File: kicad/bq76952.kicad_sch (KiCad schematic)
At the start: 88 parts, among them Q1 DMN10H220LE, U4 BQ76952

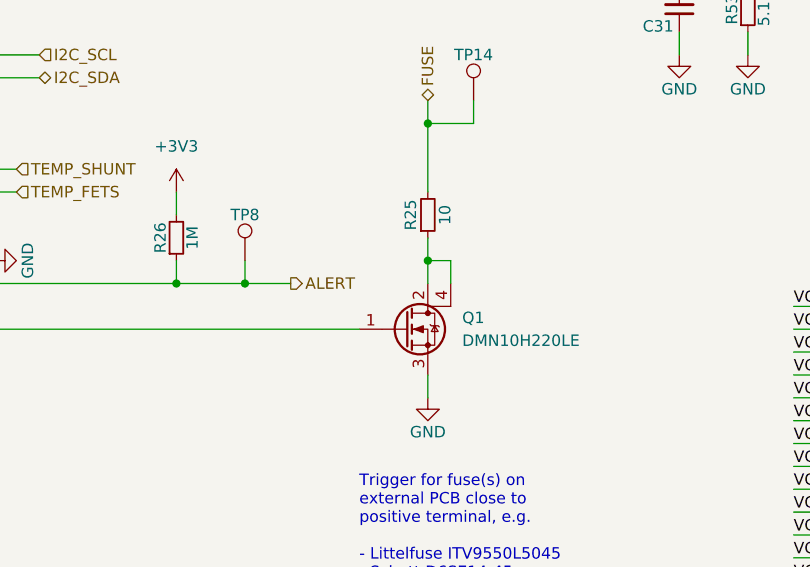
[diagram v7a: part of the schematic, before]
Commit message: Create cost-optimized Lite variant of the BMS C1 v0.4.1
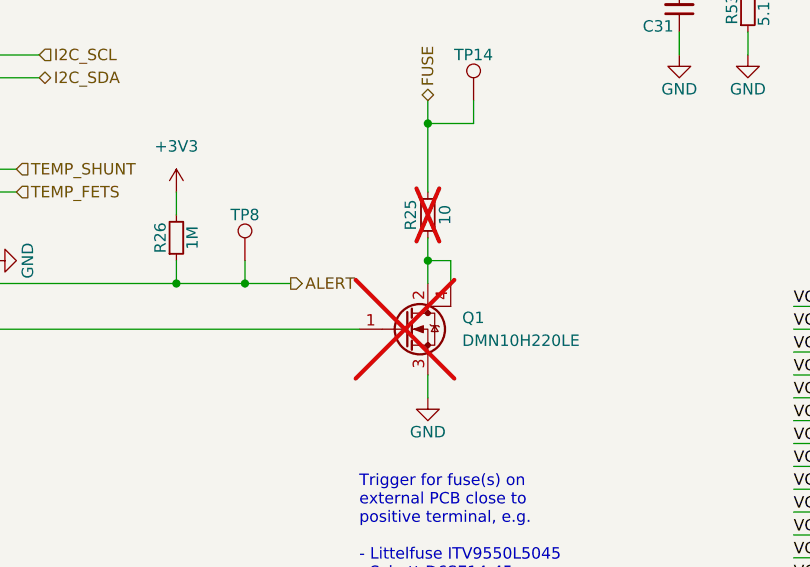
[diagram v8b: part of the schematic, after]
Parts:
- Q1, R25: now not fitted
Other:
- title: Libre Solar BMS C1 -> Libre Solar BMS C1 lite
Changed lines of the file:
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@@
 	(paper "A4")
 	(title_block
-		(title "Libre Solar BMS C1")
+		(title "Libre Solar BMS C1 lite")
 		(date "2024-03-17")
 		(rev "0.4.1")
@@
 		(exclude_from_sim no)
 		(in_bom yes)
-		(on_board yes)
-		(dnp no)
+		(on_board no)
+		(dnp yes)
 		(property "Reference" "Q1"
 			(at 204.47 115.5699 0)
@@
 		(exclude_from_sim no)
 		(in_bom yes)
-		(on_board yes)
+		(on_board no)
 		(dnp no)
 		(property "Reference" "TP14"
@@
 		(exclude_from_sim no)
 		(in_bom yes)
-		(on_board yes)
-		(dnp no)
+		(on_board no)
+		(dnp yes)
 		(property "Reference" "R25"
 			(at 198.755 104.14 90)
